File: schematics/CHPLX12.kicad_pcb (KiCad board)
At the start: 2 copper layers, 19 parts, among them J1 Conn_01x04

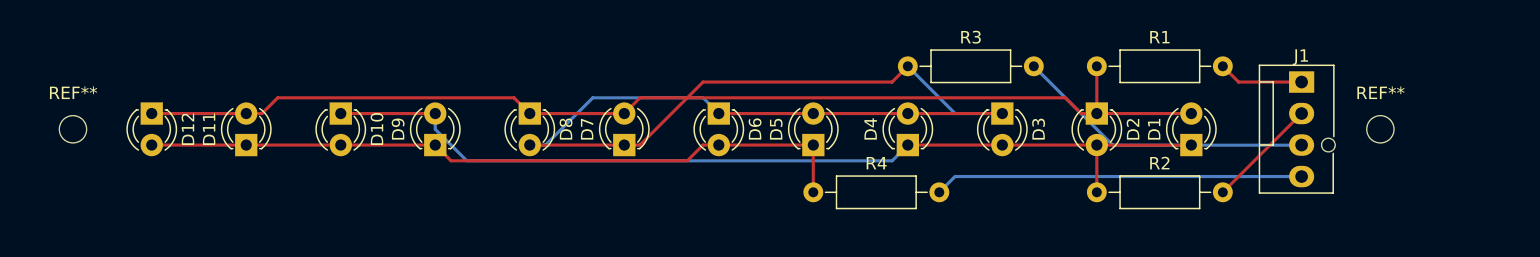
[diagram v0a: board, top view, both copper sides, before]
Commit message: add display pcb design with gerber files
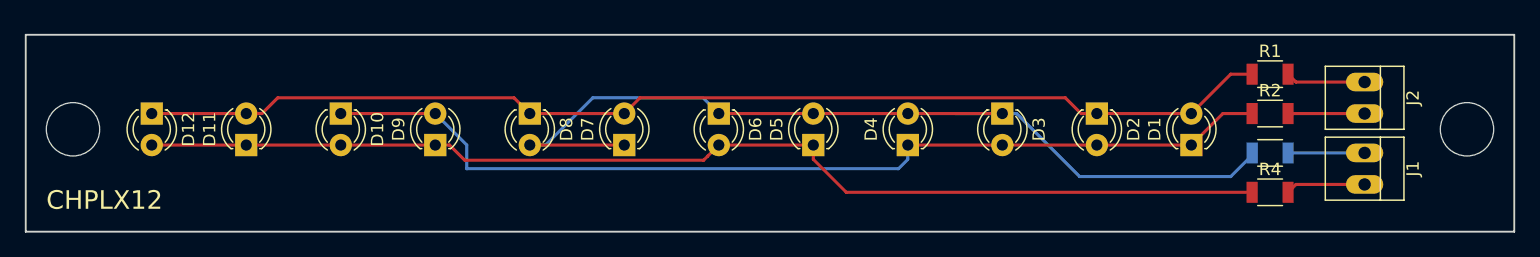
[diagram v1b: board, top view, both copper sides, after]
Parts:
- removed REF** (x2): MountingHole_2.2mm_M2_DIN965, Mounting_Holes:MountingHole_2.2mm_M2_DIN965
- added ?: , Mounting_Holes:MountingHole_4.3mm_M4_DIN965, F.Cu at (38.1, 74.9)
- added ?: , Mounting_Holes:MountingHole_4.3mm_M4_DIN965, F.Cu at (150.5, 74.9)
- added J2: , Connectors:PINHEAD1-2, F.Cu at (142.2, 71.1)
- J1: value Conn_01x04 -> (none); footprint Connectors:Fan_Pin_Header_Straight_1x04 -> Connectors:PINHEAD1-2
- R1, R2, R3, R4: value R -> 220; footprint Resistors_THT:R_Axial_DIN0207_L6.3mm_D2.5mm_P10.16mm_Horizontal -> Resistors_SMD:R_1206
- moved R4 36.8 mm to (134.6, 80.0)
- moved R3 30.0 mm to (134.6, 76.8)
- moved R2 15.3 mm to (134.6, 73.7)
- moved R1 14.0 mm to (134.6, 70.5)
- moved J1 7.65 mm to (142.2, 76.8), turned to 270 degrees
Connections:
- J1 pad 1: PIN1 -> PIN3
- J1 pad 2: PIN2 -> PIN4
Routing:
- net Net-(D10-Pad2): track 58.2 -> 92.0 mm
- net PIN4: track 29.7 -> 6.43 mm
- net PIN3: track 24.2 -> 6.35 mm
- net Net-(D3-Pad1): track 82.5 -> 74.8 mm
- net Net-(D1-Pad1): track 75.2 -> 79.0 mm
- net PIN2: track 8.98 -> 6.17 mm
- net Net-(D1-Pad2): track 89.7 -> 92.1 mm
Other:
- board outline added: 120 x 15.9 mm
- rule trace_min: 0.2 -> 0.25
- board text added: "CHPLX12"

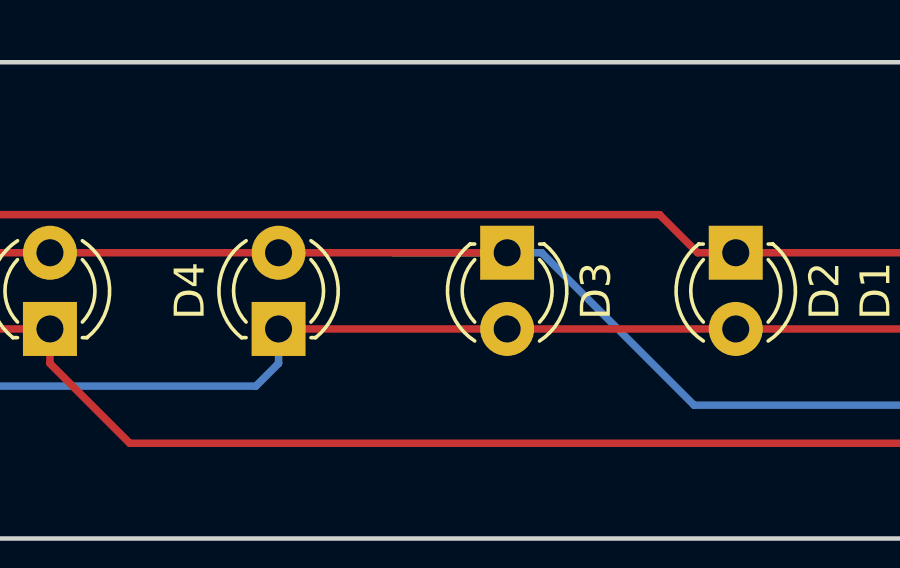
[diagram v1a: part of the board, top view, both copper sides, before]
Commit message: remove unnecessary wire from pcb
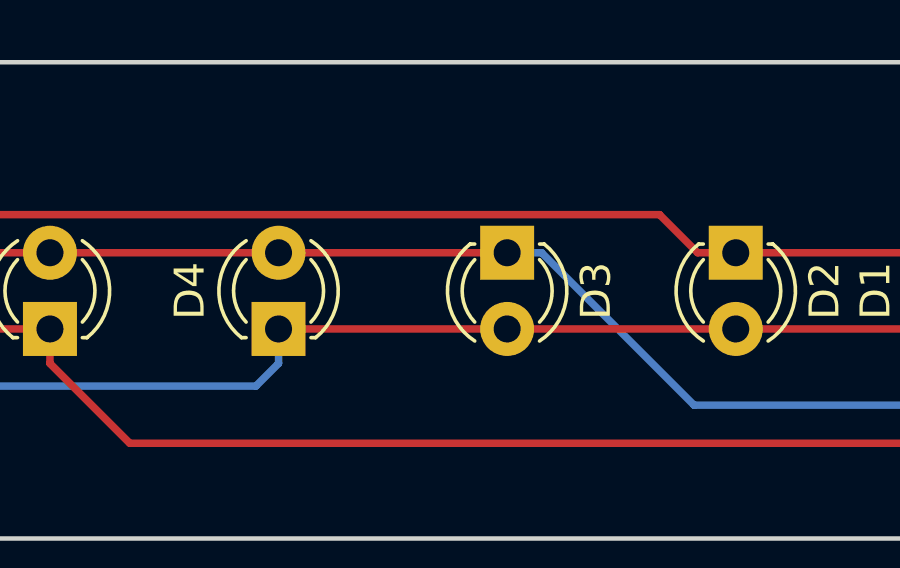
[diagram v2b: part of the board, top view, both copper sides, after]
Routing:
- net Net-(D3-Pad1): track 74.8 -> 71.0 mm
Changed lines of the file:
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@@
     (thickness 1.6)
     (drawings 5)
-    (tracks 55)
+    (tracks 54)
     (zones 0)
     (modules 20)
@@
     (34 B.Paste user hide)
     (35 F.Paste user hide)
-    (36 B.SilkS user hide)
+    (36 B.SilkS user)
     (37 F.SilkS user)
-    (38 B.Mask user hide)
-    (39 F.Mask user hide)
+    (38 B.Mask user)
+    (39 F.Mask user)
     (40 Dwgs.User user hide)
     (41 Cmts.User user hide)
@@
       (drillshape 0)
       (scaleselection 1)
-      (outputdirectory "plot/"))
+      (outputdirectory "gerber/"))
   )
   (net 0 "")
@@
   (segment (start 97.79 73.66) (end 105.41 73.66) (width 0.25) (layer F.Cu) (net 3))
   (segment (start 113.03 73.66) (end 105.41 73.66) (width 0.25) (layer F.Cu) (net 3))
-  (segment (start 113.03 73.66) (end 109.22 73.66) (width 0.25) (layer B.Cu) (net 3))
   (segment (start 131.445 78.74) (end 133.35 76.835) (width 0.25) (layer B.Cu) (net 3))
   (segment (start 119.26 78.74) (end 131.445 78.74) (width 0.25) (layer B.Cu) (net 3))
